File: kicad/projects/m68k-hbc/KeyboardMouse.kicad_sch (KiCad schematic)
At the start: 15 parts

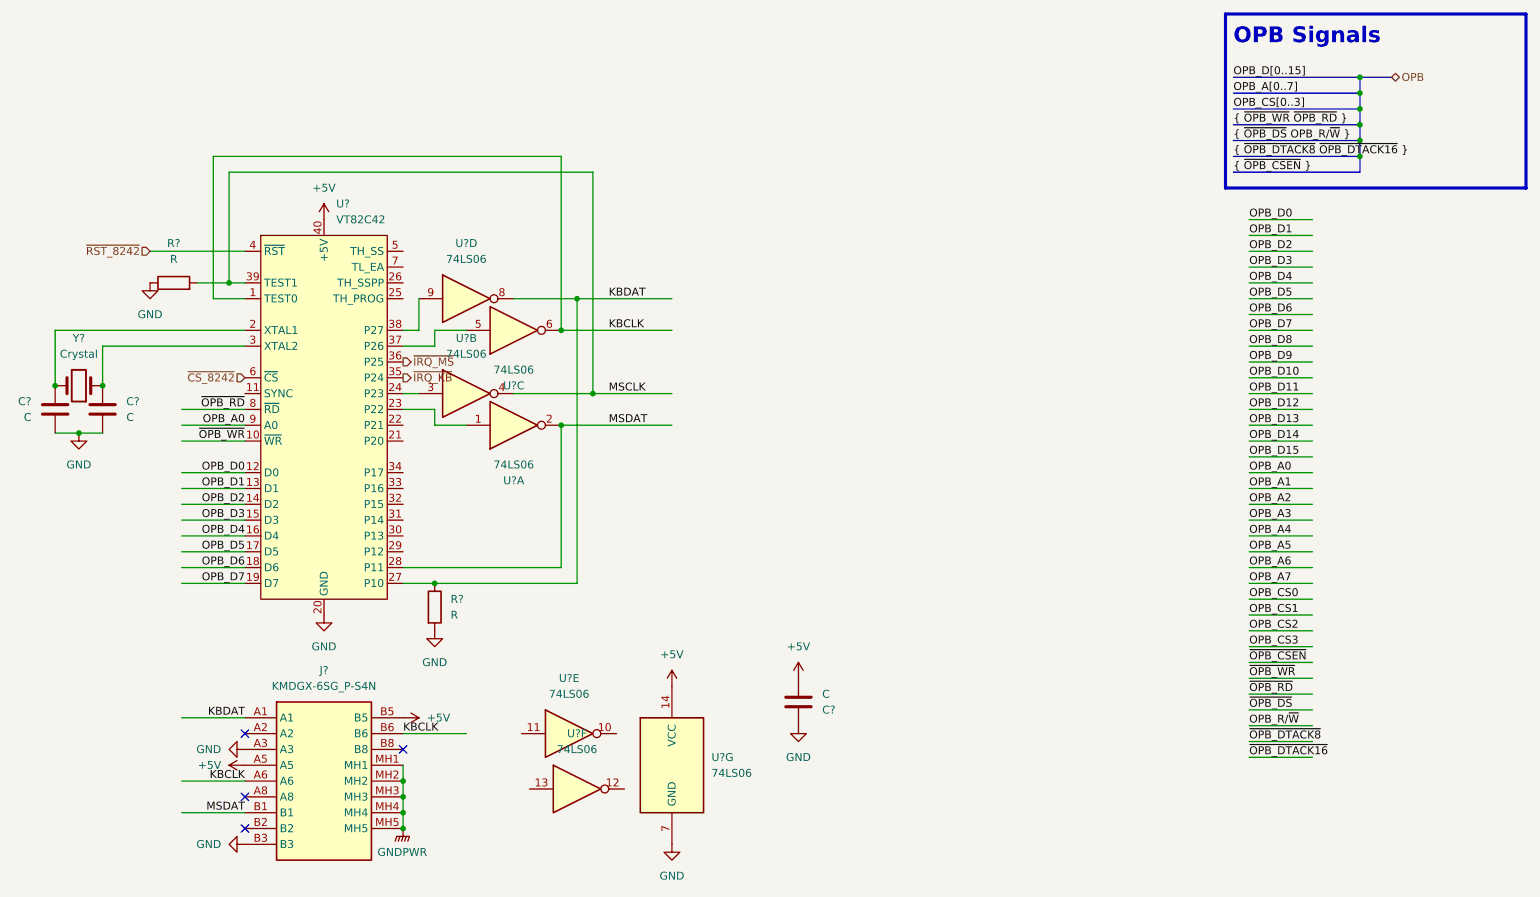
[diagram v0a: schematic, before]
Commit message: Large changes: EHBCSimpleEmu, kicad, fwcode, docs
This commit contains some large changes:
- Removed EHBCSimpleEmu (Moved to kms1212/llemu, kms1212/qemu)
- (likely) Removed fwcode; now it only boots and stops
- Modified documents
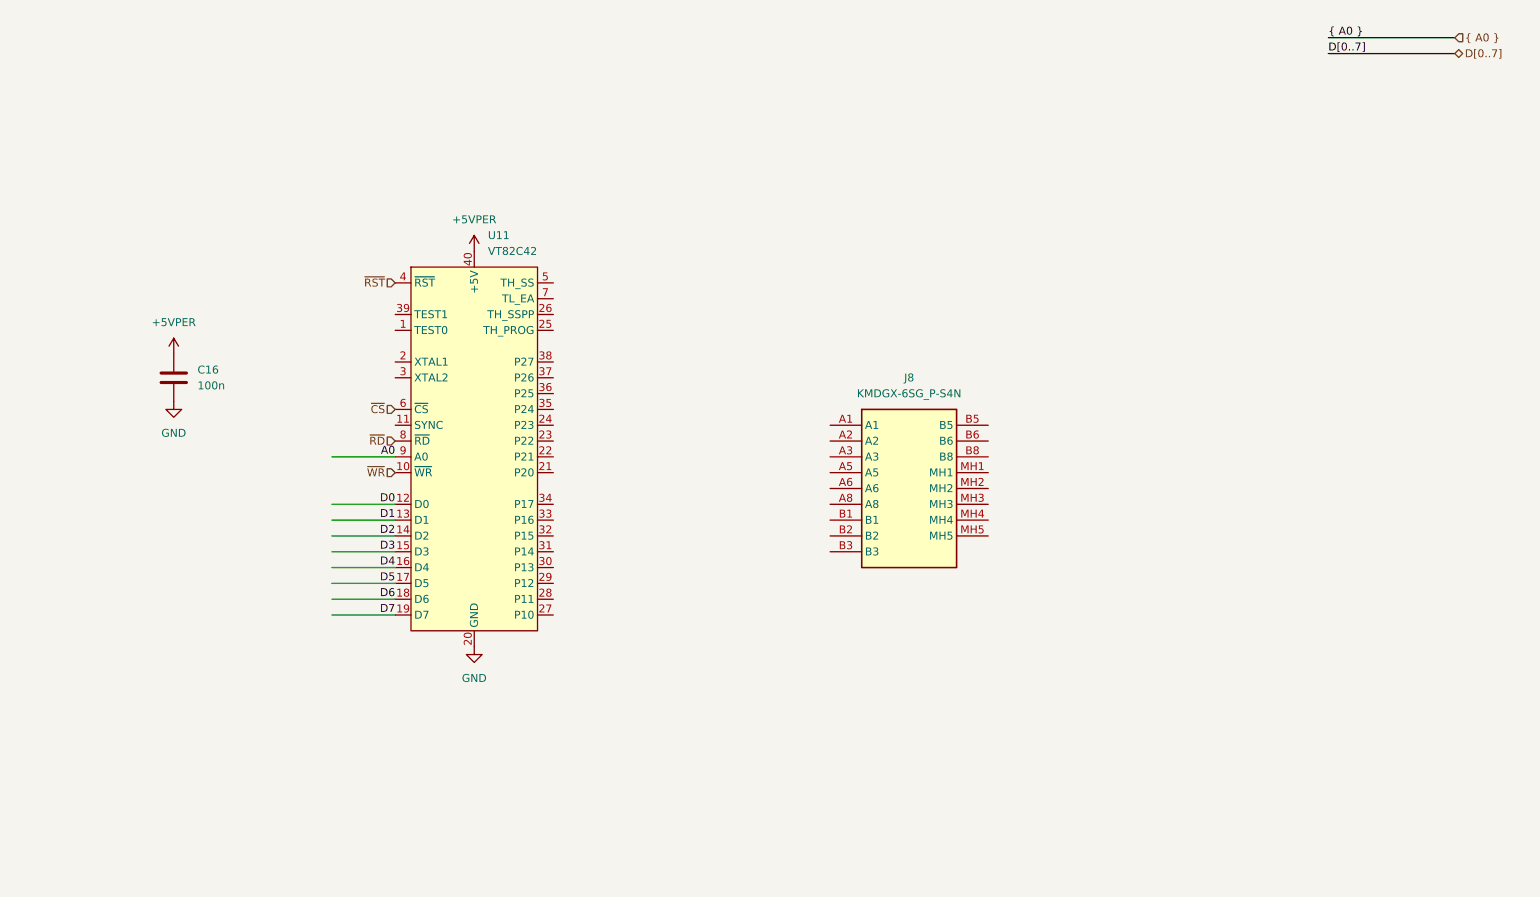
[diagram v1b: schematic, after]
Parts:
- removed C? (x3): C, Capacitor_SMD:C_0603_1608Metric_Pad1.08x0.95mm_HandSolder, symbol Device:C
- removed J?: KMDGX-6SG_P-S4N, KMDGX6SGPS4N, symbol KMDGX-6SG_P-S4N:KMDGX-6SG_P-S4N
- removed R? (x2): R, Resistor_SMD:R_0603_1608Metric_Pad0.98x0.95mm_HandSolder, symbol Device:R
- removed U? (x7): 74LS06, Package_SO:SOIC-14W_7.5x9mm_P1.27mm, symbol 74xx:74LS06
- removed U?: VT82C42, Package_DIP:DIP-40_W15.24mm_Socket, symbol VT82C42:VT82C42
- removed Y?: Crystal, Crystal:Crystal_HC52-6mm_Vertical, symbol Device:Crystal
- added C16: 100n, Capacitor_THT:C_Disc_D6.0mm_W2.5mm_P5.00mm, symbol Device:C
- added J8: KMDGX-6SG_P-S4N, KMDGX6SGPS4N:KMDGX6SGPS4N, symbol KMDGX-6SG_P-S4N:KMDGX-6SG_P-S4N
- added U11: VT82C42, Package_DIP:DIP-40_W15.24mm_Socket, symbol m68k-hbc-ic:VT82C42
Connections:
- net GND: now also C16.2, U11.20 (GND)
- new net +5VPER: C16.1, U11.40 (+5V)
- new net A0: U11.9 (A0)
- new net D0: U11.12 (D0)
- new net D1: U11.13 (D1)
- new net D2: U11.14 (D2)
- new net D3: U11.15 (D3)
- new net D4: U11.16 (D4)
- new net D5: U11.17 (D5)
- new net D6: U11.18 (D6)
- new net D7: U11.19 (D7)
- new net ~{CS}: U11.6 (~{CS})
- new net ~{RD}: U11.8 (~{RD})
- new net ~{RST}: U11.4 (~{RST})
- new net ~{WR}: U11.10 (~{WR})
- no-connect marks 4 -> 0
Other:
- note removed: "OPB Signals"
